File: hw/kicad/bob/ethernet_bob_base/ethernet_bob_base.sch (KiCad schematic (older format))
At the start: 8 parts, among them J1 DB9_Male, J2 Conn_01x02_Male, U2 TJA1021T, U3 MCP2551-I-SN, U4 MC33879A, U5 MC33879A

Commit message: add outputs
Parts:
- added J3, J4: Conn_01x02_Male, stmbl-kicad-lib:RM3.5_1x2_UP, symbol Connector:Conn_01x02_Male
- added J5, J6: Conn_01x06_Male, stmbl-kicad-lib:RM3.5_1x6_UP, symbol Connector:Conn_01x06_Male
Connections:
- net at U4.10 (S1): now also J5.6 (Pin_6)
- net VD: now reaches U4.11 (D1)
- net VD: now also U4.22 (D3), U4.26 (D4), U4.28 (D7), U4.31 (VPWR), U4.5 (D8), U4.7 (D2), U5.11 (D1), U5.22 (D3), U5.26 (D4), U5.28 (D7), U5.31 (VPWR), U5.5 (D8), U5.7 (D2)
- net at U4.12 (D6): now also U4.23 (S3), J3.2 (Pin_2)
- net at U4.13 (S6): now also J5.3 (Pin_3)
- net at U4.20 (S5): now also J5.4 (Pin_4)
- net at U4.21 (D5): now also U4.27 (S4), J3.1 (Pin_1)
- net at U4.29 (S7): now also J5.2 (Pin_2)
- net at U4.3 (S8): now also J5.1 (Pin_1)
- net HSDRV_DO: now reaches U4.32 (DO), U5.17 (DI)
- net at U4.6 (S2): now also J5.5 (Pin_5)
- net at U5.10 (S1): now also J6.1 (Pin_1)
- net at U5.12 (D6): now also U5.23 (S3), J4.2 (Pin_2)
- net at U5.13 (S6): now also J6.4 (Pin_4)
- net at U5.20 (S5): now also J6.3 (Pin_3)
- net at U5.21 (D5): now also U5.27 (S4), J4.1 (Pin_1)
- net at U5.29 (S7): now also J6.5 (Pin_5)
- net at U5.3 (S8): now also J6.6 (Pin_6)
- net at U5.6 (S2): now also J6.2 (Pin_2)

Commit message: routing
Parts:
- removed J5, J6: Conn_01x06_Male, stmbl-kicad-lib:RM3.5_1x6_UP, symbol Connector:Conn_01x06_Male
- added J5, J6, J7, J8: Conn_01x04_Male, stmbl-kicad-lib:RM3.5_1x4_UP, symbol Connector:Conn_01x04_Male
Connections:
- net GND: now also U4.13 (S6), U4.20 (S5), U5.13 (S6), U5.20 (S5), J8.1 (Pin_1), J8.2 (Pin_2), J8.3 (Pin_3), J8.4 (Pin_4)
- net VD: now also J7.1 (Pin_1), J7.2 (Pin_2), J7.3 (Pin_3), J7.4 (Pin_4)
- net at U4.3 (S8): now also J5.1 (Pin_1)
- net at U4.29 (S7): now also J5.4 (Pin_4)
- net at U4.6 (S2): now also J5.2 (Pin_2)
- net at U4.10 (S1): now also J5.3 (Pin_3)
- net at U5.10 (S1): now also J6.3 (Pin_3)
- net at U5.6 (S2): now also J6.2 (Pin_2)
- net at U5.29 (S7): now also J6.4 (Pin_4)
- net at U5.3 (S8): now also J6.1 (Pin_1)
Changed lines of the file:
@@
 Wire Wire Line
 	9150 1750 9150 1450
-$Comp
-L Connector:Conn_01x06_Male J5
-U 1 1 5C99F589
-P 10550 2550
-F 0 "J5" H 10522 2432 50  0000 R CNN
-F 1 "Conn_01x06_Male" H 10522 2523 50  0000 R CNN
-F 2 "stmbl-kicad-lib:RM3.5_1x6_UP" H 10550 2550 50  0001 C CNN
-F 3 "~" H 10550 2550 50  0001 C CNN
-	1    10550 2550
-	-1   0    0    1
-$EndComp
 Wire Wire Line
 	8950 2750 10350 2750
 Wire Wire Line
-	8950 2650 10350 2650
-Wire Wire Line
-	8950 2550 10350 2550
-Wire Wire Line
-	8950 2450 10350 2450
-Wire Wire Line
 	8950 2150 10050 2150
-Wire Wire Line
-	10050 2150 10050 2350
-Wire Wire Line
-	10050 2350 10350 2350
 Wire Wire Line
 	8950 2050 10150 2050
 Wire Wire Line
-	10150 2050 10150 2250
-Wire Wire Line
-	10150 2250 10350 2250
-$Comp
-L Connector:Conn_01x06_Male J6
-U 1 1 5C9B383F
-P 10550 5150
-F 0 "J6" H 10522 5124 50  0000 R CNN
-F 1 "Conn_01x06_Male" H 10522 5033 50  0000 R CNN
-F 2 "stmbl-kicad-lib:RM3.5_1x6_UP" H 10550 5150 50  0001 C CNN
-F 3 "~" H 10550 5150 50  0001 C CNN
-	1    10550 5150
-	-1   0    0    -1
-$EndComp
-Wire Wire Line
 	8950 5450 10350 5450
-Wire Wire Line
-	8950 5350 10350 5350
-Wire Wire Line
-	8950 5250 10350 5250
-Wire Wire Line
-	8950 5150 10350 5150
 Wire Wire Line
 	8950 4850 10050 4850
 Wire Wire Line
-	10050 4850 10050 5050
-Wire Wire Line
-	10050 5050 10350 5050
-Wire Wire Line
 	8950 4750 10150 4750
 Wire Wire Line
-	10150 4750 10150 4950
+	10050 2650 10350 2650
 Wire Wire Line
-	10150 4950 10350 4950
+	10050 2150 10050 2650
+Wire Wire Line
+	10150 2550 10350 2550
+Wire Wire Line
+	10150 2050 10150 2550
+Wire Wire Line
+	8950 2650 9950 2650
+Wire Wire Line
+	9950 2650 9950 2700
+Wire Wire Line
+	9950 2700 10250 2700
+Wire Wire Line
+	10250 2700 10250 2450
+Wire Wire Line
+	10250 2450 10350 2450
+Wire Wire Line
+	10050 5350 10350 5350
+Wire Wire Line
+	10050 4850 10050 5350
+Wire Wire Line
+	10150 5250 10350 5250
+Wire Wire Line
+	10150 4750 10150 5250
+Wire Wire Line
+	8950 5350 9950 5350
+Wire Wire Line
+	9950 5350 9950 5400
+Wire Wire Line
+	9950 5400 10250 5400
+Wire Wire Line
+	10250 5400 10250 5150
+Wire Wire Line
+	10250 5150 10350 5150
+$Comp
+L stmbl:GND #PWR0140
+U 1 1 5CA24125
+P 9250 2500
+F 0 "#PWR0140" H 9250 2250 50  0001 C CNN
+F 1 "GND" V 9255 2372 50  0000 R CNN
+F 2 "" H 9250 2500 50  0001 C CNN
+F 3 "" H 9250 2500 50  0001 C CNN
+	1    9250 2500
+	0    -1   -1   0
+$EndComp
+Wire Wire Line
+	8950 2450 9050 2450
+Wire Wire Line
+	9050 2450 9050 2500
+Wire Wire Line
+	9050 2550 8950 2550
+Wire Wire Line
+	9050 2500 9250 2500
+Connection ~ 9050 2500
+Wire Wire Line
+	9050 2500 9050 2550
+$Comp
+L stmbl:GND #PWR0141
+U 1 1 5CA2FF2F
+P 9250 5200
+F 0 "#PWR0141" H 9250 4950 50  0001 C CNN
+F 1 "GND" V 9255 5072 50  0000 R CNN
+F 2 "" H 9250 5200 50  0001 C CNN
+F 3 "" H 9250 5200 50  0001 C CNN
+	1    9250 5200
+	0    -1   -1   0
+$EndComp
+Wire Wire Line
+	8950 5150 9050 5150
+Wire Wire Line
+	9050 5150 9050 5200
+Wire Wire Line
+	9050 5250 8950 5250
+Wire Wire Line
+	9050 5200 9250 5200
+Connection ~ 9050 5200
+Wire Wire Line
+	9050 5200 9050 5250
+$Comp
+L Connector:Conn_01x04_Male J5
+U 1 1 5CA35FF6
+P 10550 2650
+F 0 "J5" H 10522 2532 50  0000 R CNN
+F 1 "Conn_01x04_Male" H 10522 2623 50  0000 R CNN
+F 2 "stmbl-kicad-lib:RM3.5_1x4_UP" H 10550 2650 50  0001 C CNN
+F 3 "~" H 10550 2650 50  0001 C CNN
+	1    10550 2650
+	-1   0    0    1
+$EndComp
+$Comp
+L Connector:Conn_01x04_Male J6
+U 1 1 5CA3C255
+P 10550 5350
+F 0 "J6" H 10522 5232 50  0000 R CNN
+F 1 "Conn_01x04_Male" H 10522 5323 50  0000 R CNN
+F 2 "stmbl-kicad-lib:RM3.5_1x4_UP" H 10550 5350 50  0001 C CNN
+F 3 "~" H 10550 5350 50  0001 C CNN
+	1    10550 5350
+	-1   0    0    1
+$EndComp
+$Comp
+L Connector:Conn_01x04_Male J7
+U 1 1 5CA8B49E
+P 5650 5800
+F 0 "J7" H 5622 5682 50  0000 R CNN
+F 1 "Conn_01x04_Male" H 5622 5773 50  0000 R CNN
+F 2 "stmbl-kicad-lib:RM3.5_1x4_UP" H 5650 5800 50  0001 C CNN
+F 3 "~" H 5650 5800 50  0001 C CNN
+	1    5650 5800
+	-1   0    0    1
+$EndComp
+$Comp
+L Connector:Conn_01x04_Male J8
+U 1 1 5CA8B995
+P 5650 6300
+F 0 "J8" H 5622 6182 50  0000 R CNN
+F 1 "Conn_01x04_Male" H 5622 6273 50  0000 R CNN
+F 2 "stmbl-kicad-lib:RM3.5_1x4_UP" H 5650 6300 50  0001 C CNN
+F 3 "~" H 5650 6300 50  0001 C CNN
+	1    5650 6300
+	-1   0    0    1
+$EndComp
+$Comp
+L stmbl:GND #PWR0144
+U 1 1 5CA94A36
+P 5350 6500
+F 0 "#PWR0144" H 5350 6250 50  0001 C CNN
+F 1 "GND" H 5355 6327 50  0000 C CNN
+F 2 "" H 5350 6500 50  0001 C CNN
+F 3 "" H 5350 6500 50  0001 C CNN
+	1    5350 6500
+	1    0    0    -1
+$EndComp
+Wire Wire Line
+	5450 6100 5350 6100
+Wire Wire Line
+	5350 6100 5350 6200
+Wire Wire Line
+	5450 6400 5350 6400
+Connection ~ 5350 6400
+Wire Wire Line
+	5350 6400 5350 6500
+Wire Wire Line
+	5450 6300 5350 6300
+Connection ~ 5350 6300
+Wire Wire Line
+	5350 6300 5350 6400
+Wire Wire Line
+	5450 6200 5350 6200
+Connection ~ 5350 6200
+Wire Wire Line
+	5350 6200 5350 6300
+Wire Wire Line
+	5450 5900 5350 5900
+Wire Wire Line
+	5350 5900 5350 5800
+Wire Wire Line
+	5450 5600 5350 5600
+Connection ~ 5350 5600
+Wire Wire Line
+	5350 5600 5350 5500
+Wire Wire Line
+	5450 5700 5350 5700
+Connection ~ 5350 5700
+Wire Wire Line
+	5350 5700 5350 5600
+Wire Wire Line
+	5450 5800 5350 5800
+Connection ~ 5350 5800
+Wire Wire Line
+	5350 5800 5350 5700
+$Comp
+L stmbl:VD #PWR0145
+U 1 1 5CAC0B79
+P 5350 5500
+F 0 "#PWR0145" H 5350 5350 50  0001 C CNN
+F 1 "VD" H 5367 5673 50  0000 C CNN
+F 2 "" H 5350 5500 50  0001 C CNN
+F 3 "" H 5350 5500 50  0001 C CNN
+	1    5350 5500
+	1    0    0    -1
+$EndComp
 $EndSCHEMATC

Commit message: routing...
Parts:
- added C18, C19, C20, C21, C22, C23, C24, C25, C26, C27, C28, C29, C30, C31, C32, C33: C, stmbl-kicad-lib:C_0805, symbol stmbl:C
- added H1, H2, H3, H4: MountingHole_Pad, Mounting_Holes:MountingHole_3.2mm_M3_Pad_Via, symbol Mechanical:MountingHole_Pad
- added J10, J11, J12, J9: Conn_01x04_Male, stmbl-kicad-lib:RM3.5_1x4_UP, symbol Connector:Conn_01x04_Male
- added R10, R11, R12, R13, R14, R15, R16, R17, R18, R19, R20, R21, R22, R23, R24, R25, R26, R27, R28, R29, R30, R31, R32, R33, R34, R35, R36, R37, R38, R7, R8, R9: R, stmbl-kicad-lib:R_0603, symbol stmbl:R
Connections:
- net GND: now also C18.2, C19.2, C20.2, C21.2, C22.2, C23.2, C24.2, C25.2, C26.2, C27.2, C28.2, C29.2, C30.2, C31.2, C32.2, C33.2, H1.1, H2.1, H3.1, H4.1, R23.2, R24.2, R25.2, R26.2, R27.2, R28.2, R29.2, R30.2, R31.2, R32.2, R33.2, R34.2, R35.2, R36.2, R37.2, R38.2
- new net: J9.1 (Pin_1), R7.2
- new net: J9.2 (Pin_2), R8.2
- new net: J9.3 (Pin_3), R9.2
- new net: J9.4 (Pin_4), R10.2
- new net: J10.1 (Pin_1), R11.2
- new net: J10.2 (Pin_2), R12.2
- new net: J10.3 (Pin_3), R13.2
- new net: J10.4 (Pin_4), R14.2
- new net: J11.1 (Pin_1), R15.2
- new net: J11.2 (Pin_2), R16.2
- new net: J11.3 (Pin_3), R17.2
- new net: J11.4 (Pin_4), R18.2
- new net: J12.1 (Pin_1), R19.2
- new net: J12.2 (Pin_2), R20.2
- new net: J12.3 (Pin_3), R21.2
- new net: J12.4 (Pin_4), R22.2
- new net ADC0: C18.1, R23.1, R7.1
- new net ADC1: C22.1, R27.1, R8.1
- new net ADC10: C28.1, R17.1, R33.1
- new net ADC11: C32.1, R18.1, R37.1
- new net ADC12: C21.1, R19.1, R26.1
- new net ADC13: C25.1, R20.1, R30.1
- new net ADC14: C29.1, R21.1, R34.1
- new net ADC15: C33.1, R22.1, R38.1
- new net ADC2: C26.1, R31.1, R9.1
- new net ADC3: C30.1, R10.1, R35.1
- new net ADC4: C19.1, R11.1, R24.1
- new net ADC5: C23.1, R12.1, R28.1
- new net ADC6: C27.1, R13.1, R32.1
- new net ADC7: C31.1, R14.1, R36.1
- new net ADC8: C20.1, R15.1, R25.1
- new net ADC9: C24.1, R16.1, R29.1

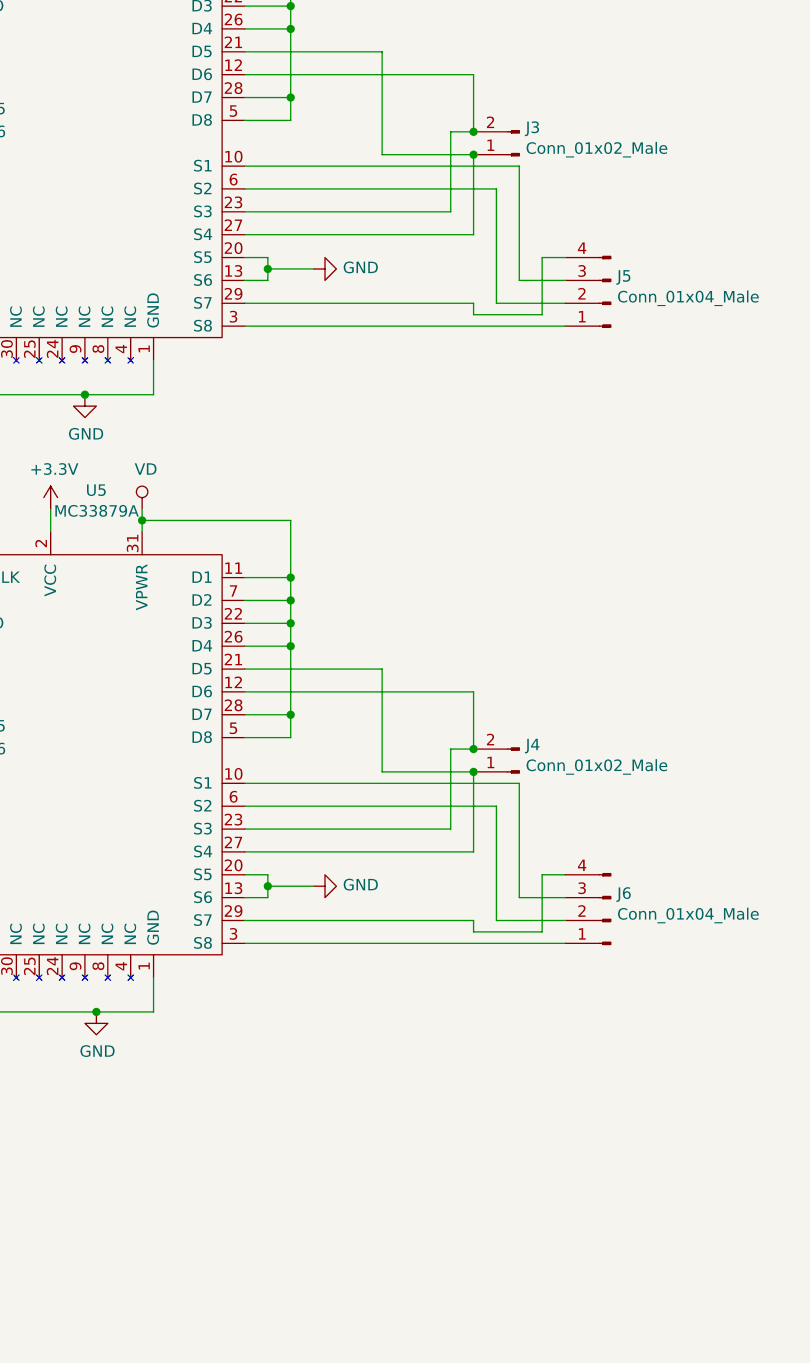
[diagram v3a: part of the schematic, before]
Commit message: add leds
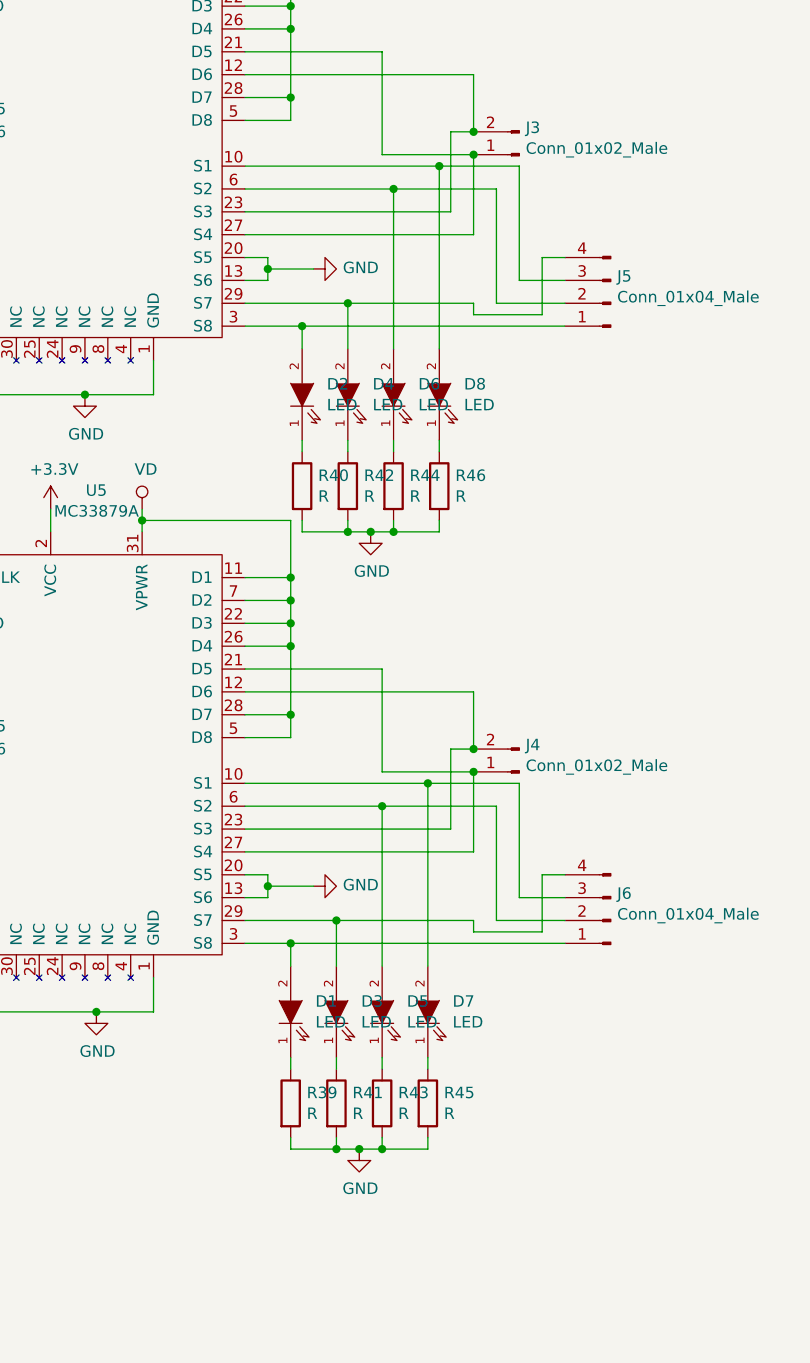
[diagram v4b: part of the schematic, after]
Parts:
- added D1, D2, D3, D4, D5, D6, D7, D8: LED, stmbl-kicad-lib:LED-0805, symbol stmbl:LED
- added R39, R40, R41, R42, R43, R44, R45, R46: R, stmbl-kicad-lib:R_0603, symbol stmbl:R
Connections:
- net GND: now also R39.2, R40.2, R41.2, R42.2, R43.2, R44.2, R45.2, R46.2
- net at J5.3 (Pin_3), U4.10 (S1): now also D8.2 (A)
- net at J5.4 (Pin_4), U4.29 (S7): now also D4.2 (A)
- net at J5.1 (Pin_1), U4.3 (S8): now also D2.2 (A)
- net at J5.2 (Pin_2), U4.6 (S2): now also D6.2 (A)
- net at J6.3 (Pin_3), U5.10 (S1): now also D7.2 (A)
- net at J6.4 (Pin_4), U5.29 (S7): now also D3.2 (A)
- net at J6.1 (Pin_1), U5.3 (S8): now also D1.2 (A)
- net at J6.2 (Pin_2), U5.6 (S2): now also D5.2 (A)
- new net: D1.1 (K), R39.1
- new net: D3.1 (K), R41.1
- new net: D5.1 (K), R43.1
- new net: D7.1 (K), R45.1
- new net: D2.1 (K), R40.1
- new net: D4.1 (K), R42.1
- new net: D6.1 (K), R44.1
- new net: D8.1 (K), R46.1
